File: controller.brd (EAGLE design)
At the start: 61 x 38.1 mm, 26 parts, among them U1 ATMEGA328P_PDIP

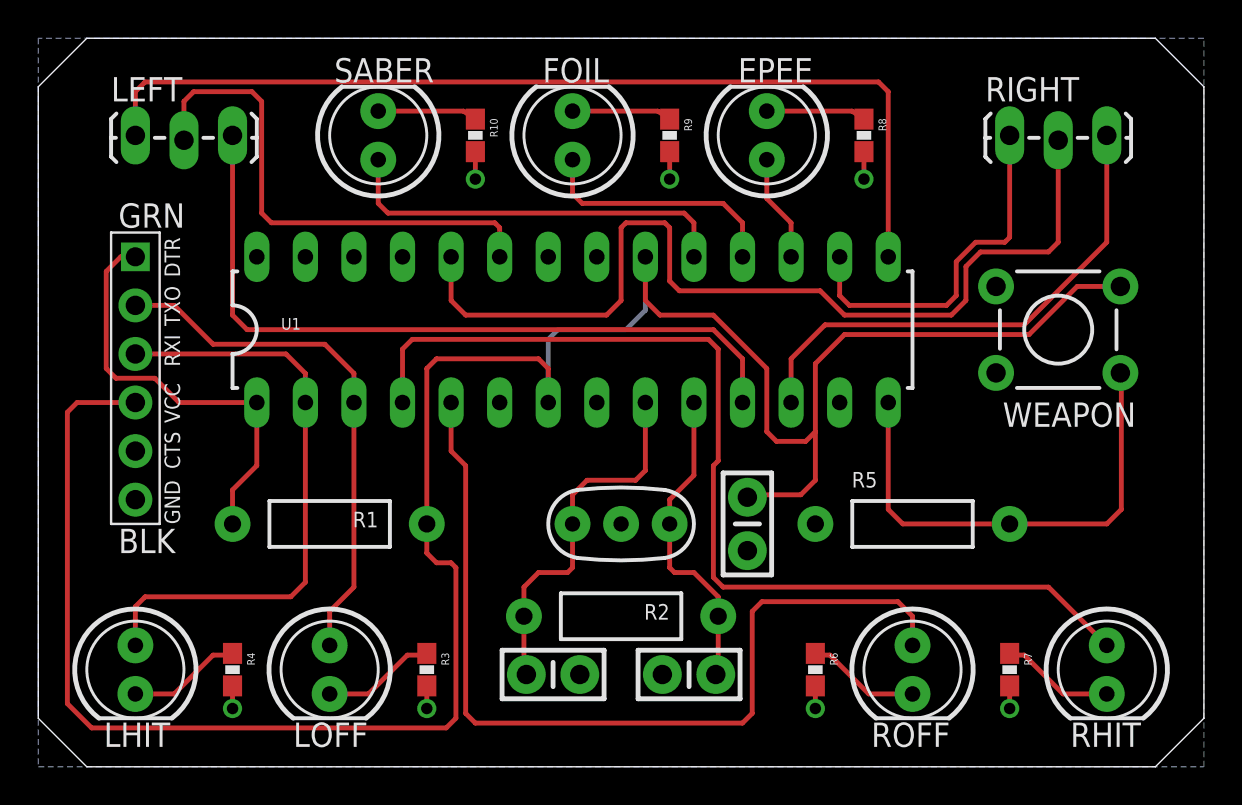
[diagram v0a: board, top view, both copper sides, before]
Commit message: Fixed part values and modified silkscreen
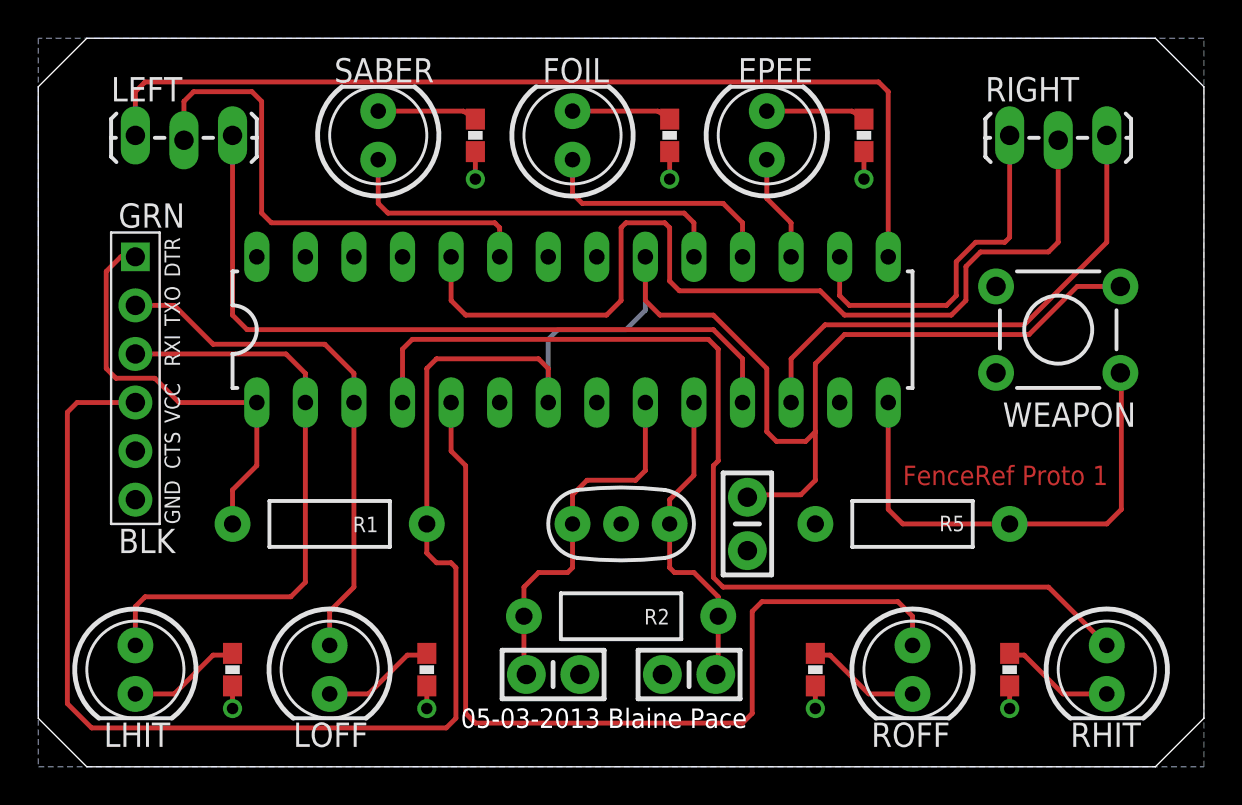
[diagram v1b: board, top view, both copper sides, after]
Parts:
- R5: value (none) -> 10k
- Y1: value (none) -> 16MHz
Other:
- board text added: "05-03-2013 Blaine Pace"
- board text added: "FenceRef Proto 1"
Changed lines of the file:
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@@
 <wire x1="2.54" y1="0" x2="0" y2="2.54" width="0" layer="20"/>
 <wire x1="0" y1="2.54" x2="0" y2="35.56" width="0" layer="20"/>
+<text x="45.212" y="14.732" size="1.016" layer="1">FenceRef Proto 1</text>
+<text x="22.098" y="2.032" size="1.016" layer="20">05-03-2013 Blaine Pace</text>
 </plain>
 <attributes>
@@
 </autorouter>
 <elements>
-<element name="U1" library="SparkFun-DigitalIC" package="DIL28-3" value="ATMEGA328P_PDIP" x="27.94" y="22.86"/>
+<element name="U1" library="SparkFun-DigitalIC" package="DIL28-3" value="ATMEGA328P_PDIP" x="27.94" y="22.86" smashed="yes"/>
 <element name="C1" library="SparkFun-Capacitors" package="CAP-PTH-SMALL-KIT" value="0.1uF" x="37.084" y="12.7" rot="R270"/>
 <element name="R1" library="SparkFun-Resistors" package="AXIAL-0.4" value="10k" x="15.24" y="12.7" smashed="yes" rot="R180">
-<attribute name="NAME" x="17.78" y="13.335" size="0.8128" layer="25" font="vector" ratio="15" rot="R180"/>
+<attribute name="NAME" x="17.78" y="13.081" size="0.8128" layer="25" font="vector" ratio="15" rot="R180"/>
 </element>
 <element name="R2" library="SparkFun-Resistors" package="AXIAL-0.4" value="10k" x="30.48" y="7.874" smashed="yes" rot="R180">
-<attribute name="NAME" x="33.02" y="8.509" size="0.8128" layer="25" font="vector" ratio="15" rot="R180"/>
-</element>
-<element name="Y1" library="SparkFun-FreqCtrl" package="RESONATOR-PTH" value="" x="30.48" y="12.7"/>
+<attribute name="NAME" x="33.02" y="8.255" size="0.8128" layer="25" font="vector" ratio="15" rot="R180"/>
+</element>
+<element name="Y1" library="SparkFun-FreqCtrl" package="RESONATOR-PTH" value="16MHz" x="30.48" y="12.7"/>
 <element name="C2" library="SparkFun-Capacitors" package="CAP-PTH-SMALL-KIT" value="22pF" x="26.924" y="4.826"/>
 <element name="C3" library="SparkFun-Capacitors" package="CAP-PTH-SMALL-KIT" value="22pF" x="34.036" y="4.826" rot="R180"/>
@@
 <attribute name="NAME" x="57.404" y="19.05" size="1.27" layer="25" ratio="10" rot="R180"/>
 </element>
-<element name="R5" library="SparkFun-Resistors" package="AXIAL-0.4" value="" x="45.72" y="12.7"/>
+<element name="R5" library="SparkFun-Resistors" package="AXIAL-0.4" value="10k" x="45.72" y="12.7" smashed="yes">
+<attribute name="NAME" x="47.117" y="12.319" size="0.8128" layer="25" font="vector" ratio="15"/>
+</element>
 <element name="JP1" library="SparkFun-Connectors" package="FTDI_DEVICE_SIDE" value="FTDI_DEVICE" x="5.08" y="20.32" rot="R270"/>
-<element name="R6" library="SparkFun-Resistors" package="0603-RES" value="330" x="40.64" y="5.08" rot="R270"/>
-<element name="R7" library="SparkFun-Resistors" package="0603-RES" value="330" x="50.8" y="5.08" rot="R270"/>
-<element name="R3" library="SparkFun-Resistors" package="0603-RES" value="330" x="20.32" y="5.08" rot="R270"/>
-<element name="R4" library="SparkFun-Resistors" package="0603-RES" value="330" x="10.16" y="5.08" rot="R270"/>
-<element name="R8" library="SparkFun-Resistors" package="0603-RES" value="330" x="43.18" y="33.02" rot="R270"/>
-<element name="R9" library="SparkFun-Resistors" package="0603-RES" value="330" x="33.02" y="33.02" rot="R270"/>
-<element name="R10" library="SparkFun-Resistors" package="0603-RES" value="330" x="22.86" y="33.02" rot="R270"/>
+<element name="R6" library="SparkFun-Resistors" package="0603-RES" value="330" x="40.64" y="5.08" smashed="yes" rot="R270"/>
+<element name="R7" library="SparkFun-Resistors" package="0603-RES" value="330" x="50.8" y="5.08" smashed="yes" rot="R270"/>
+<element name="R3" library="SparkFun-Resistors" package="0603-RES" value="330" x="20.32" y="5.08" smashed="yes" rot="R270"/>
+<element name="R4" library="SparkFun-Resistors" package="0603-RES" value="330" x="10.16" y="5.08" smashed="yes" rot="R270"/>
+<element name="R8" library="SparkFun-Resistors" package="0603-RES" value="330" x="43.18" y="33.02" smashed="yes" rot="R270"/>
+<element name="R9" library="SparkFun-Resistors" package="0603-RES" value="330" x="33.02" y="33.02" smashed="yes" rot="R270"/>
+<element name="R10" library="SparkFun-Resistors" package="0603-RES" value="330" x="22.86" y="33.02" smashed="yes" rot="R270"/>
 <element name="LEFT" library="SparkFun-Connectors" package="1X03_LOCK_LONGPADS" value="" x="5.08" y="33.02"/>
 <element name="RIGHT" library="SparkFun-Connectors" package="1X03_LOCK_LONGPADS" value="" x="50.8" y="33.02"/>
